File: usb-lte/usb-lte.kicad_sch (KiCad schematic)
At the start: 48 parts, among them J1 Sim slot, P1 USB_C_Plug_USB2.0, Q1 MBT3904DW1, Q2 MBT3904DW1, U1 TPS62A02APDDC

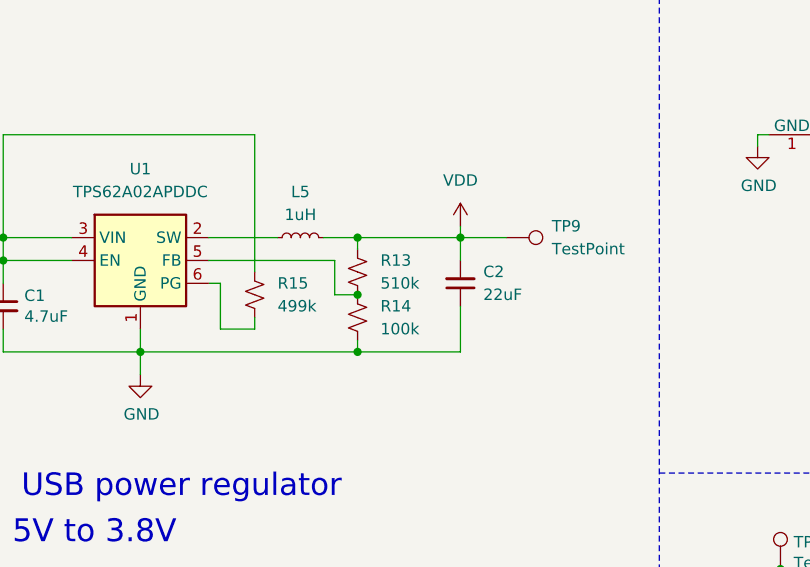
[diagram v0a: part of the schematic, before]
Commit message: Update test points
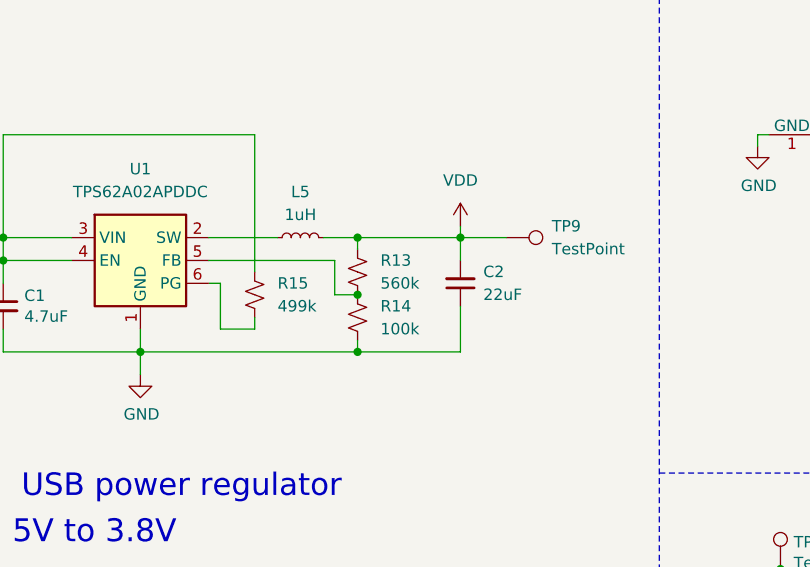
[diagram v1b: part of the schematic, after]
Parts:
- R13: value 510k -> 560k
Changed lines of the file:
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@@
 			)
 		)
-		(property "Value" "510k"
+		(property "Value" "560k"
 			(at 83.82 144.7799 0)
 			(effects

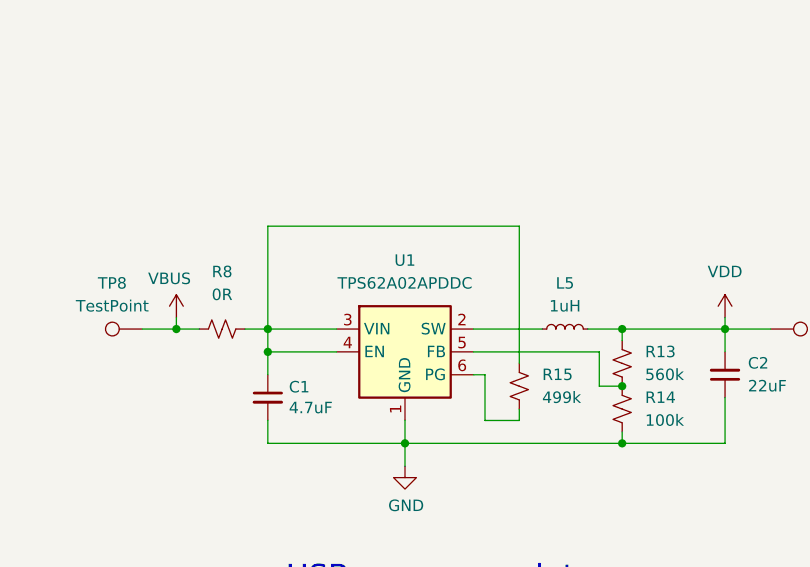
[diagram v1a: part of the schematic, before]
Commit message: Fix SMPS chip variant number
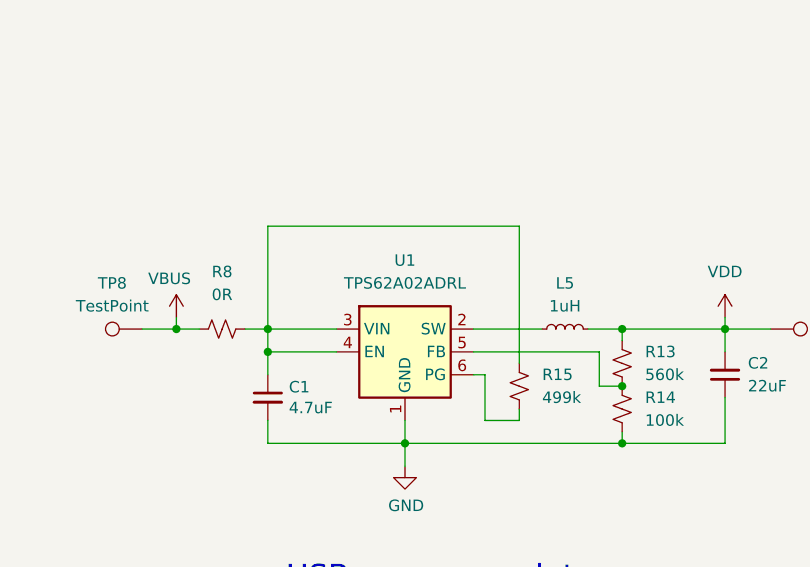
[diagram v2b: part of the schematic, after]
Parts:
- U1: value TPS62A02APDDC -> TPS62A02ADRL
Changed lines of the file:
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@@
 			)
 		)
-		(property "Value" "TPS62A02APDDC"
+		(property "Value" "TPS62A02ADRL"
 			(at 57.15 134.62 0)
 			(effects
